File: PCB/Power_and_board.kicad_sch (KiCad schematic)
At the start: 21 parts, among them U5 AMS1117-3.3

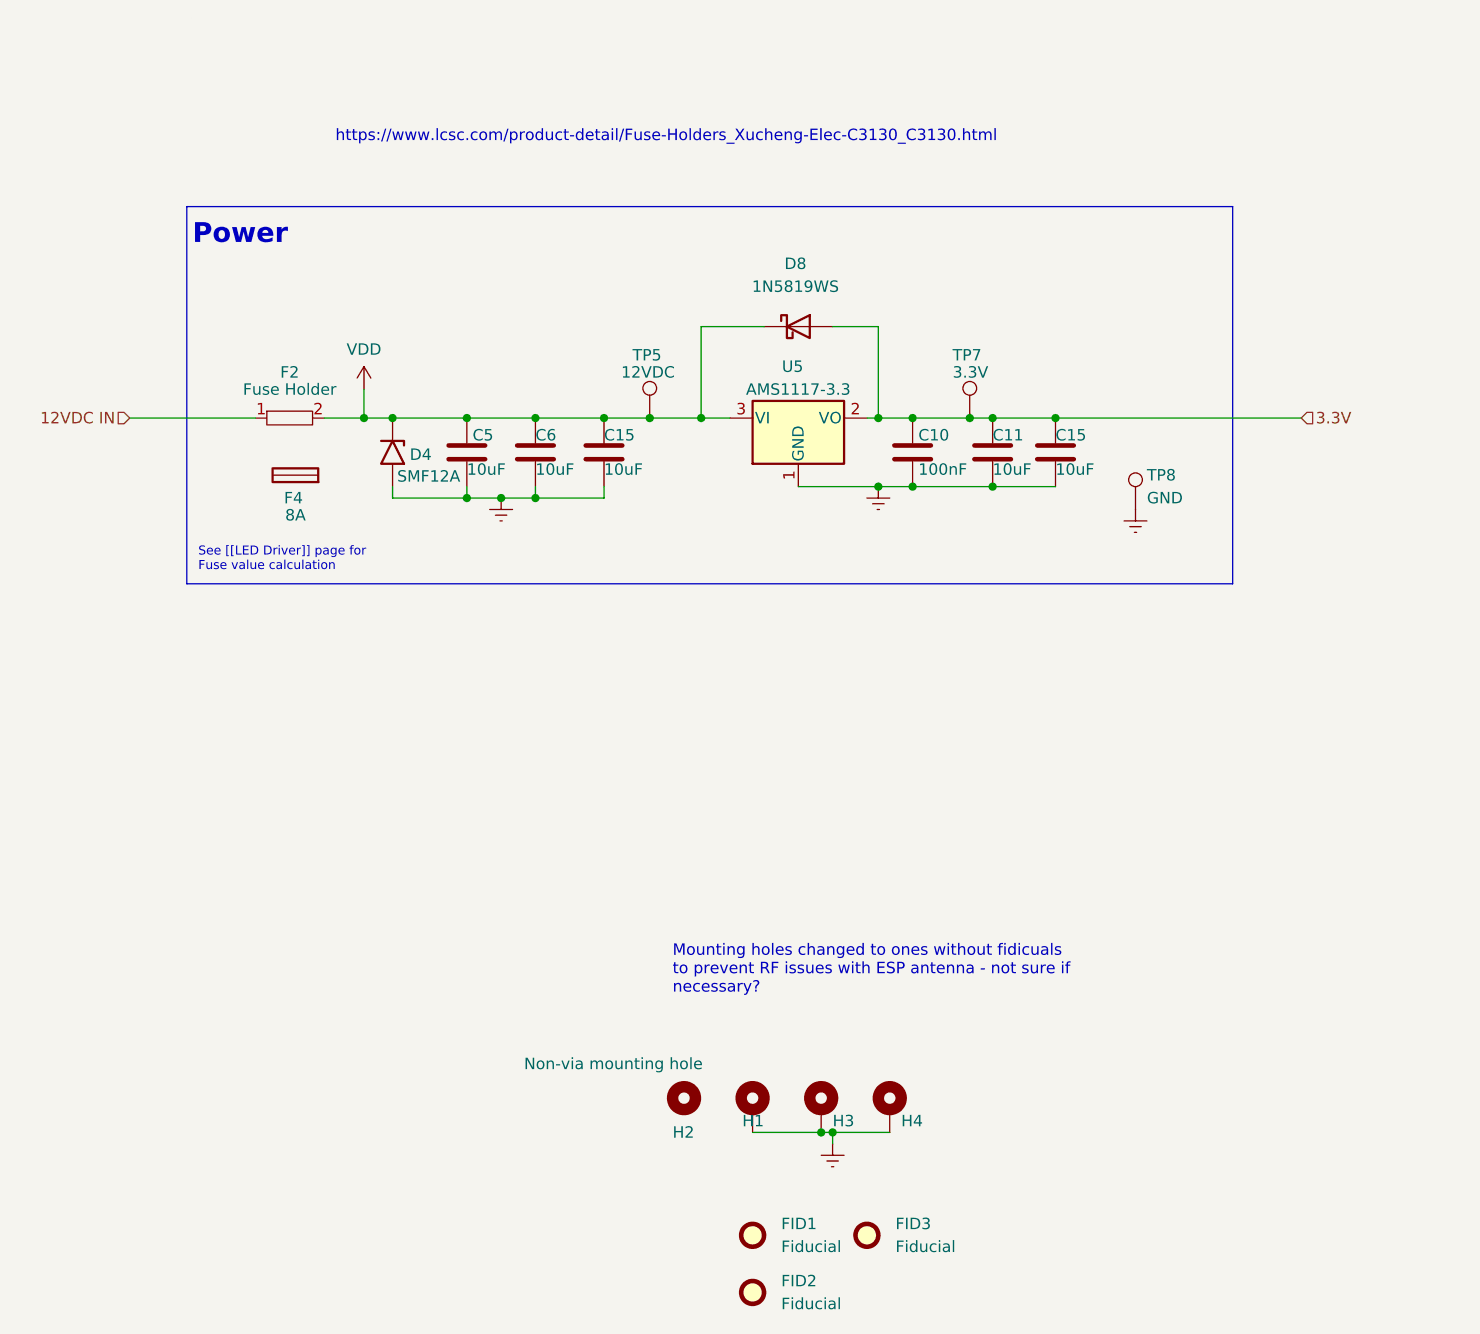
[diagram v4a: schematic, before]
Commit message: design v1.0 - complete redesign
* redid schematic
* changed to screw terminal
* added W channel for RGBW strips
* did layout
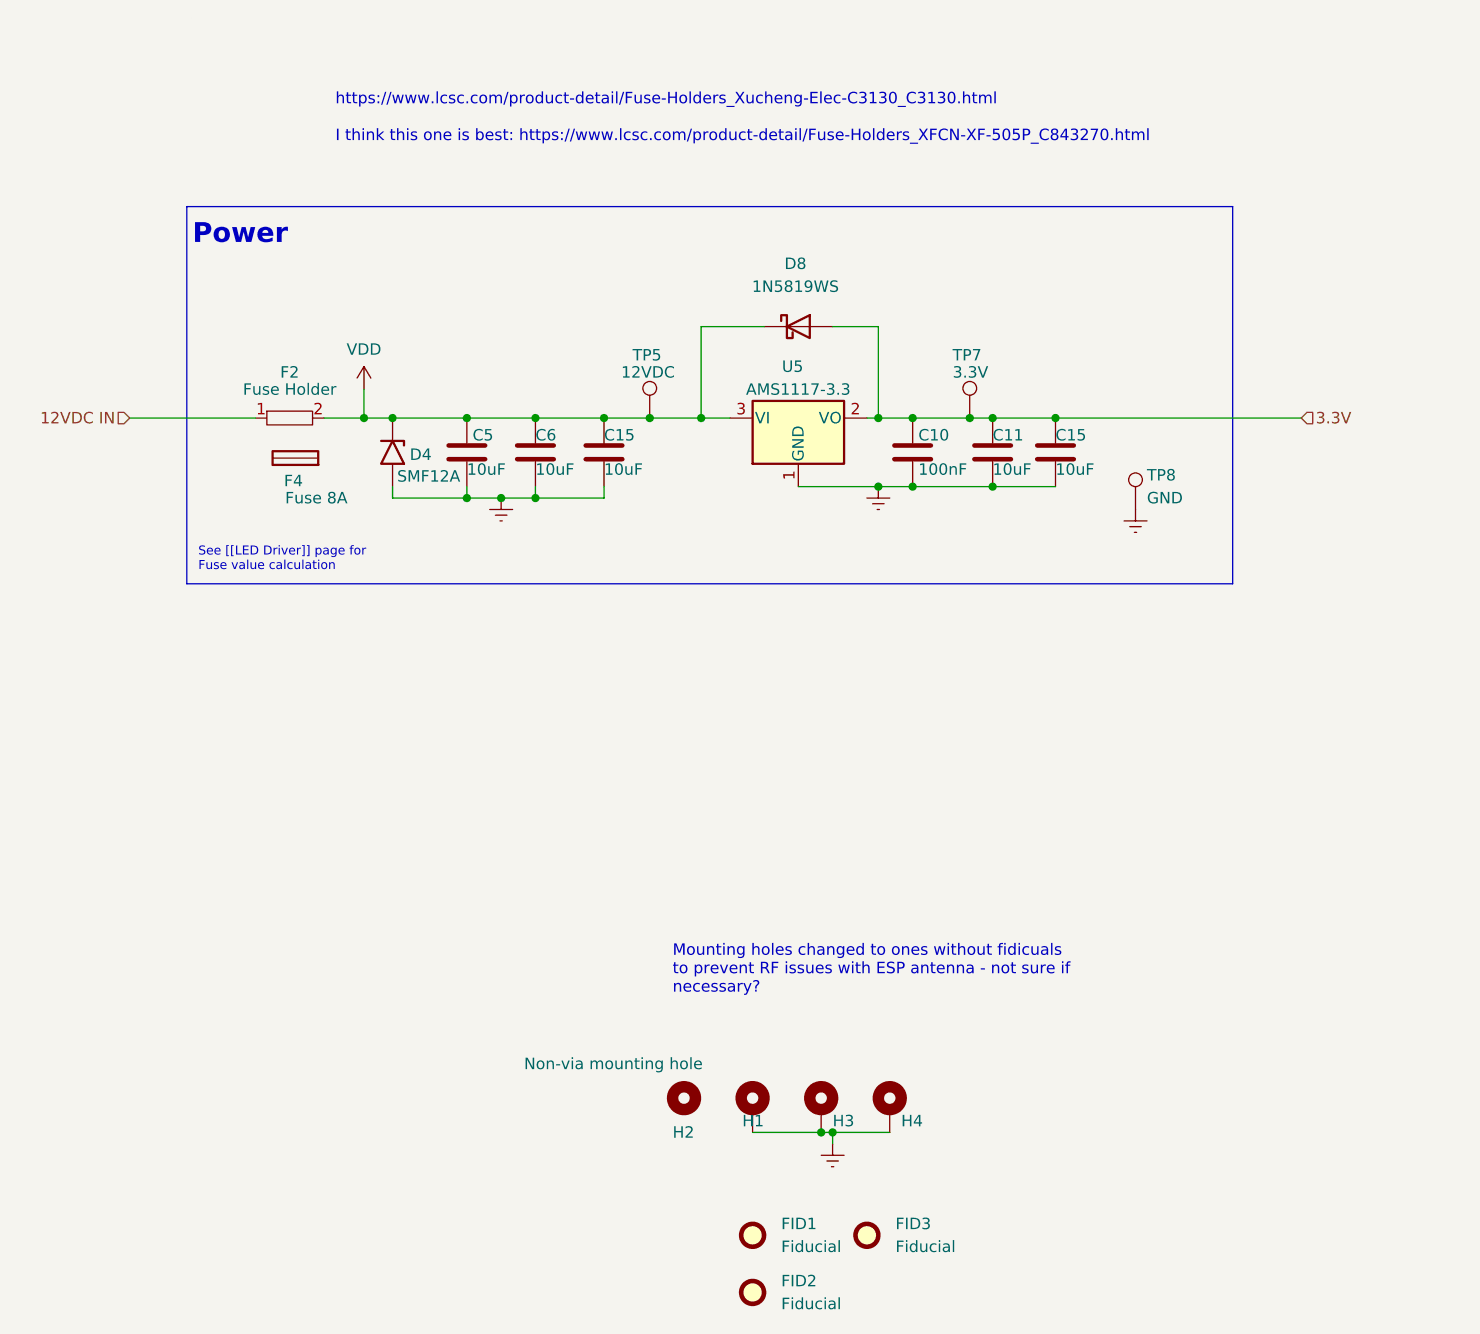
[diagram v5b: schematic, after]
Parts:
- F2: footprint Fuse:Fuseholder_Clip-5x20mm_Littelfuse_111_Inline_P20.00x5.00mm_D1.05mm_Horizontal -> projectlib:FUSE-TH_XF-505P; LCSC C2927393 -> C843270
- F4: value 8A -> Fuse 8A; LCSC (none) -> -
- FID1, FID2, FID3, H1, H2, H3, H4, TP5, TP7, TP8: LCSC (none) -> -
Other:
- note added: "https://www.lcsc.com/product-detail/Fuse-Holders_Xucheng-Elec-C3130_C3130.html I think this one is best: https://www.lcsc.com/product-detail/Fuse-Holders_XFCN-XF-505P_C843270.html"
- note removed: "https://www.lcsc.com/product-detail/Fuse-Holders_Xucheng-Elec-C3130_C3130.html"
- moved on the sheet: F4

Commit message: schematic and layout cleanup
* plus BOM finalization
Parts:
- F2: footprint projectlib:FUSE-TH_XF-505P -> jmux-footprints:FUSE-TH_XF-505P
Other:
- note removed: "Mounting holes changed to ones without fidicuals to prevent RF issues with ESP antenna - not sure if necessary?"
- note removed: "https://www.lcsc.com/product-detail/Fuse-Holders_Xucheng-Elec-C3130_C3130.html I think this one is best: https://www.lcsc.com/product-detail/Fuse-Holders_XFCN-XF-505P_C843270.html"
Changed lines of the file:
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@@
     (effects (font (size 2.2 2.2) (thickness 0.44) bold) (justify left bottom))
-  )
-  (text "Mounting holes changed to ones without fidicuals \nto prevent RF issues with ESP antenna - not sure if \nnecessary?"
-    (at 140.97 158.75 0)
-    (effects (font (size 1.27 1.27)) (justify left bottom))
-  )
-  (text "https://www.lcsc.com/product-detail/Fuse-Holders_Xucheng-Elec-C3130_C3130.html\n\nI think this one is best: https://www.lcsc.com/product-detail/Fuse-Holders_XFCN-XF-505P_C843270.html"
-    (at 103.505 64.135 0)
-    (effects (font (size 1.27 1.27)) (justify left bottom))
   )
   (hierarchical_label "3.3V" (shape input) (at 210.82 94.615 0) (fields_autoplaced)
@@
       (effects (font (size 1.27 1.27)))
     )
-    (property "Footprint" "projectlib:FUSE-TH_XF-505P" (at 99.695 100.965 0)
+    (property "Footprint" "jmux-footprints:FUSE-TH_XF-505P" (at 99.695 100.965 0)
       (effects (font (size 1.27 1.27)) hide)
     )
@@
       (effects (font (size 1.27 1.27)) (justify left))
     )
-    (property "Value" "Non-via mounting hole" (at 124.46 166.37 0)
-      (effects (font (size 1.27 1.27)) (justify left))
-    )
+    (property "Value" "Non-via mounting hole" (at 121.285 167.005 0)
+      (effects (font (size 1.27 1.27)) (justify left))
+    )
